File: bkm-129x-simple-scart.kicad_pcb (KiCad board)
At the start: 2 copper layers, 105 x 89.3 mm, 53 parts, among them J1 SCART-F, J2 RCA-RA, J5 Conn_02x32_Row_Letter_Last, Q1 DTC144EKA, U1 ADG1611, U2 THS7374, U3 arduino-nano-v3, U4 74LVC125, U5 MIC3490-3.3

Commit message: Fixed some footprints
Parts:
- added J3: RIGHT, rcj-41x:RCJ-04X, F.Cu at (122.5, 86.4)
- J2: value RCA-RA -> LEFT
- moved J2 75.8 mm to (122.5, 68.6)
- moved J1 33.8 mm to (130.7, 125.2)
- moved R30 32.1 mm to (138.6, 89.5), turned to 270 degrees
- moved R31 32.1 mm to (141.9, 89.5), turned to 90 degrees
- moved R29 32.1 mm to (135.0, 89.6), turned to 270 degrees
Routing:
- net /AUDIO_R: track 15.6 -> 65.7 mm
- net /AUDIO_L: track 27.4 -> 54.7 mm
- net Net-(C4-Pad2): track 53.1 -> 27.8 mm, vias 1 -> 0
- net Net-(C2-Pad2): track 19.8 -> 41.9 mm, vias 0 -> 1
- net Net-(C1-Pad2): track 21.2 -> 37.3 mm, vias 0 -> 1
- net Net-(C3-Pad2): track 36.2 -> 24.7 mm
- net VDD: track 88.4 -> 91.5 mm
- net /AUDIO_MONO: track 30.4 -> 32.4 mm
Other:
- board size 105 x 89.3 mm -> 105 x 90.7 mm
- board text added: "For stereo: R29,31 - Not mounted R30 - 0R (jumper)"
- board text added: "Left/Mono"
- board text added: "R1,18 - 10K R6,7,8,9 - 150R R10,11,12,13 - 75R R19,23 - 4K7 R20,22,25,27 - 100K R21,24,26,28 - 100R R29 - 470R | NM R30 - 470R | 0R R31 - 20K | NM All 0805 size"
- board text added: "Right"
- board text added: "U1 - ADG1611 U2 - THS7374 U3 - Arduino Nano v3 (5V/16MHz) U4 - 74VHC125 U5 - MIC3490-3.3 Q1 - DTC144EKA J2,3 - CUI RCJ-41X U1/2/4: TSSOP14"
- board text removed: "Mono Audio Out"
- board text removed: "R1,18 - 10K R6,7,8,9 - 150R R10,11,12,13 - 75R R19,23 - 4K7 R20,22,25,27 - 100K R21,24,26,28 - 100R R29,30 - 470R R31 - 20K All 0805 size"
- board text removed: "U1 - ADG1611 U2 - THS7374 U3 - Arduino Nano v3 (5V/16MHz) U4 - 74VHC125 U5 - MIC3490-3.3 Q1 - DTC144EKA J2 - CUI RCJ-41X U1/2/4: TSSOP14"

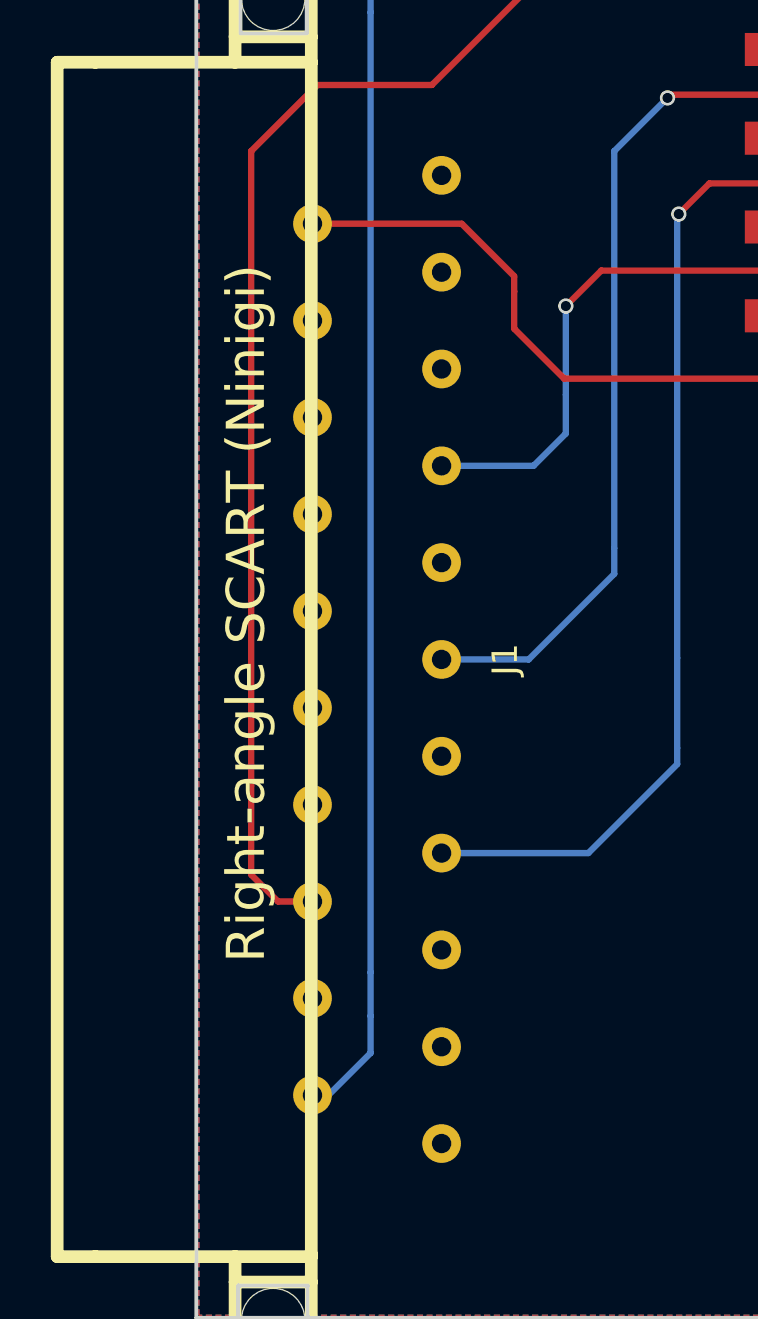
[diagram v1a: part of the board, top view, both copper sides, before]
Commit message: Fixed SCART pad size and added signal names
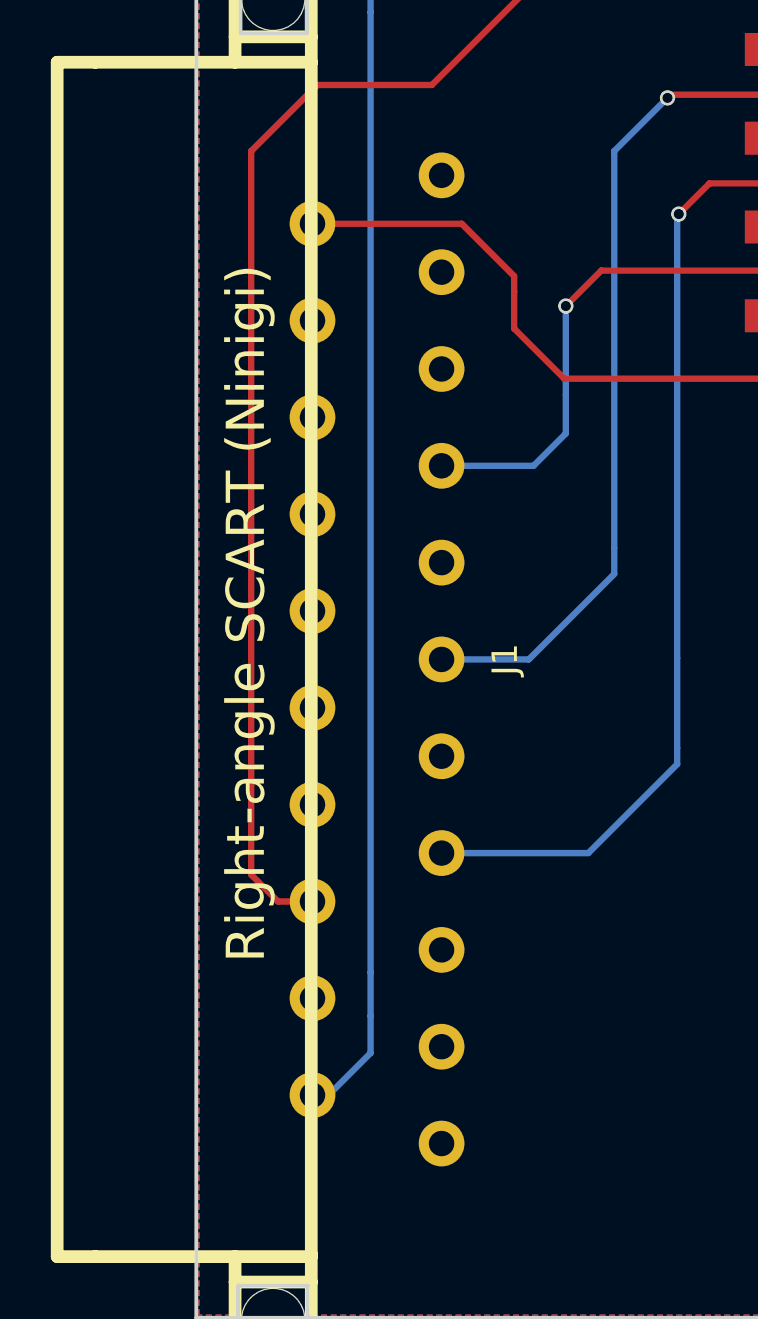
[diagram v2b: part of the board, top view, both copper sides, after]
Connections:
- net Net-(C1-Pad2) renamed /SCART_G
- net Net-(C2-Pad2) renamed /SCART_B
- net Net-(C3-Pad2) renamed /SCART_R
- net Net-(C4-Pad2) renamed /SCART_SYNC

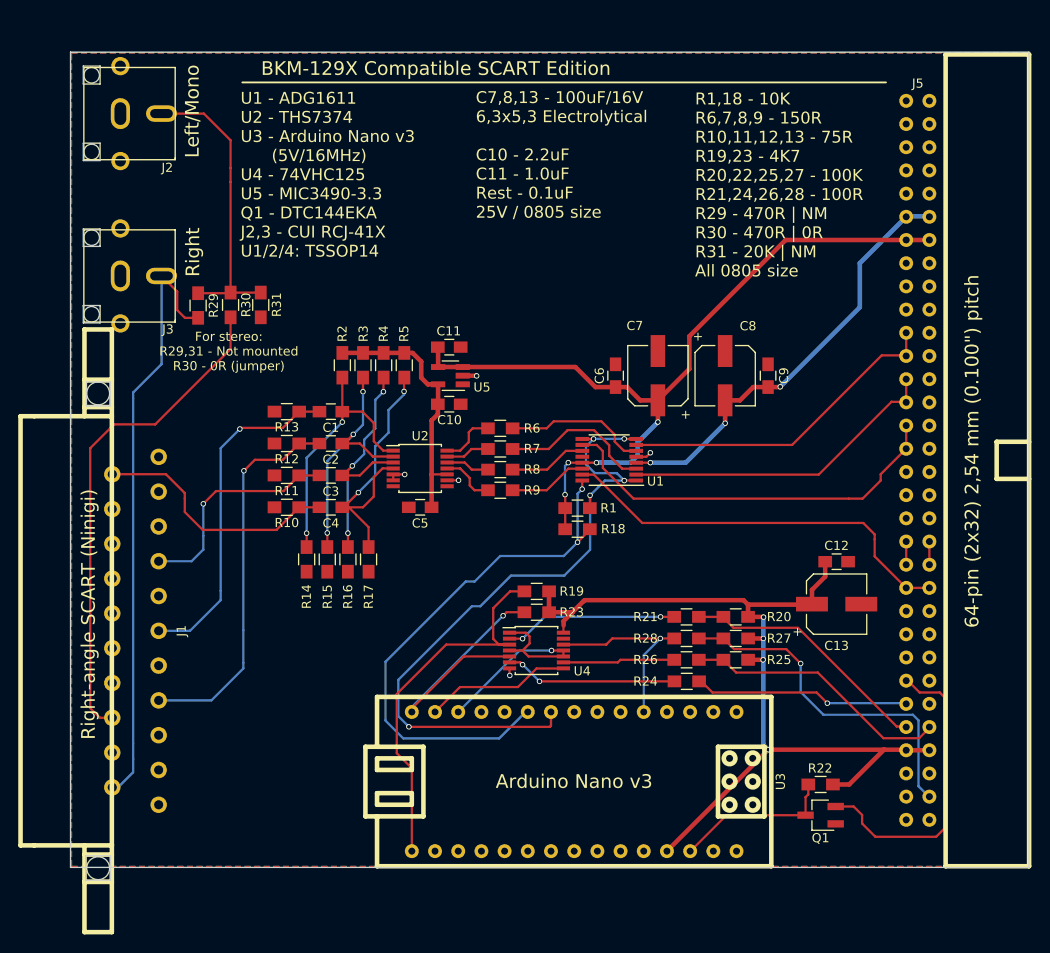
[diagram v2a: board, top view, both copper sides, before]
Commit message: Added audio switch, enlarge holes for SCART fasteners
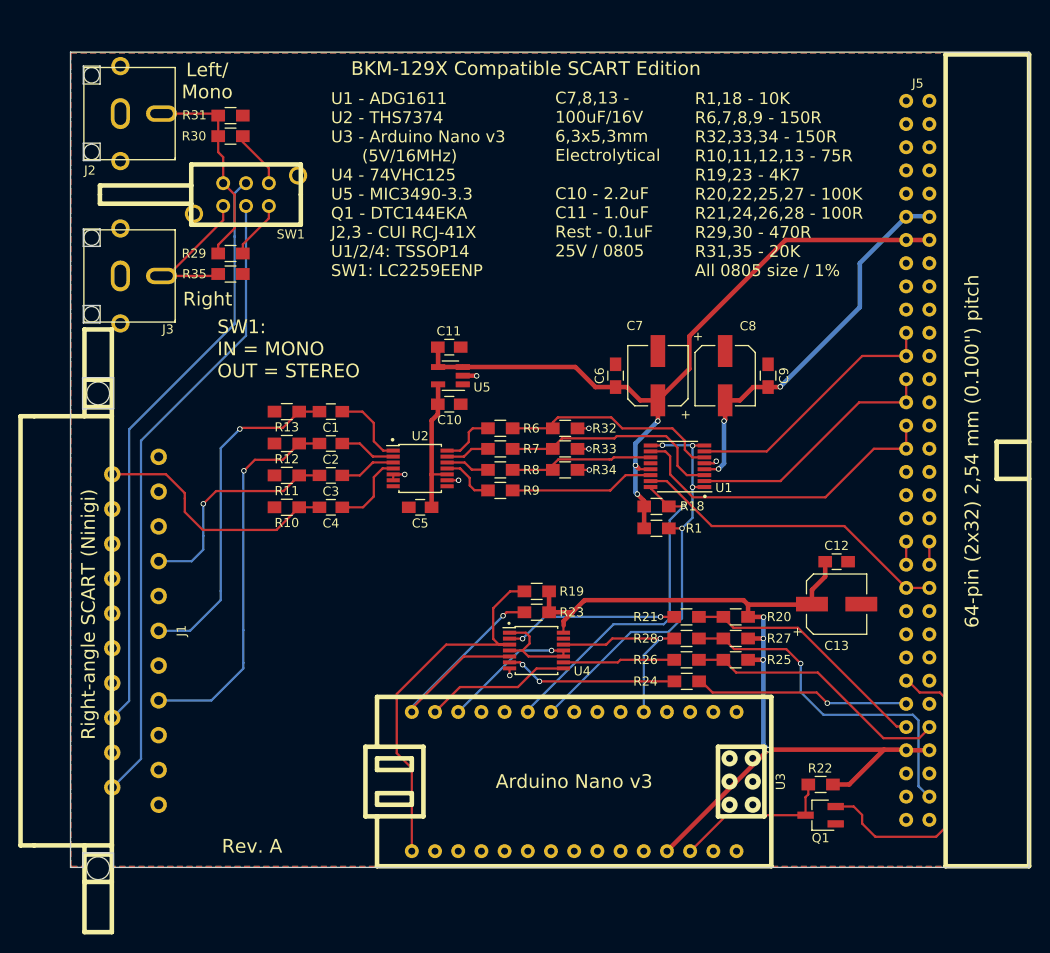
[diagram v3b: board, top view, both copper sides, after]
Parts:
- removed R14, R15, R16, R17, R2, R3, R4, R5: R, Resistors_SMD:R_0805_HandSoldering
- added R32: 150R, Resistors_SMD:R_0805_HandSoldering, F.Cu at (175.2, 103.0)
- added R33: 150R, Resistors_SMD:R_0805_HandSoldering, F.Cu at (175.2, 105.3)
- added R34: 150R, Resistors_SMD:R_0805_HandSoldering, F.Cu at (175.2, 107.6)
- added R35: 20K, Resistors_SMD:R_0805_HandSoldering, F.Cu at (138.6, 86.2)
- added SW1: LC2259EENP, LC2259:LC2259, F.Cu at (140.2, 77.5)
- R9: value 150R -> 0R
- moved R31 21.0 mm to (138.6, 68.8), turned to 180 degrees
- moved R30 18.5 mm to (138.6, 71.0), turned to 0 degrees
- moved R18 9.00 mm to (185.2, 111.6)
- moved R1 8.92 mm to (185.2, 114.0)
- moved U1 7.51 mm to (187.5, 107.2)
- moved R29 6.71 mm to (138.6, 83.9), turned to 0 degrees
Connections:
- net /AUDIO_MONO renamed Net-(J2-Pad1)
- J3 pad 1: /AUDIO_R -> Net-(J3-Pad1)
- R29 pad 2: /AUDIO_R -> Net-(R29-Pad2)
- R30 pad 2: /AUDIO_L -> Net-(R30-Pad2)
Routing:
- net ~BX_OE: track 76.7 -> 46.7 mm, vias 5 -> 4
- net Net-(C4-Pad1): track 31.6 -> 9.44 mm, vias 2 -> 0
- net ~EXT_SYNC_OE: track 59.4 -> 37.6 mm, vias 2 -> 1
- net Net-(C2-Pad1): track 28.5 -> 6.77 mm, vias 3 -> 0
- net Net-(C3-Pad1): track 27.9 -> 6.23 mm, vias 3 -> 0
- net Net-(C1-Pad1): track 28.7 -> 8.51 mm, vias 2 -> 0
- net Net-(J3-Pad1): track 0.00 -> 17.4 mm
- net +3V3: track 29.0 -> 16.0 mm
- net /AUDIO_L: track 54.7 -> 64.7 mm
- net Net-(J2-Pad1): track 32.4 -> 22.9 mm
- net /EXT_SYNC: track 44.6 -> 35.4 mm
- net Net-(R32-Pad1): track 15.6 -> 24.3 mm
- net /P-R/R: track 44.2 -> 36.0 mm
- net Net-(R33-Pad1): track 16.8 -> 24.7 mm
- net Net-(R34-Pad1): track 8.48 -> 16.0 mm
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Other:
- board size 105 x 90.7 mm -> 105 x 89.3 mm
- board text added: "C7,8,13 - 100uF/16V 6,3x5,3mm Electrolytical C10 - 2.2uF C11 - 1.0uF Rest - 0.1uF 25V / 0805"
- board text added: "Left/ Mono"
- board text added: "R1,18 - 10K R6,7,8,9 - 150R R32,33,34 - 150R R10,11,12,13 - 75R R19,23 - 4K7 R20,22,25,27 - 100K R21,24,26,28 - 100R R29,30 - 470R R31,35 - 20K All 0805 size / 1%"
- board text added: "Rev. A"
- board text added: "SW1: IN = MONO OUT = STEREO"
- board text added: "U1 - ADG1611 U2 - THS7374 U3 - Arduino Nano v3 (5V/16MHz) U4 - 74VHC125 U5 - MIC3490-3.3 Q1 - DTC144EKA J2,3 - CUI RCJ-41X U1/2/4: TSSOP14 SW1: LC2259EENP"
- board text removed: "C7,8,13 - 100uF/16V 6,3x5,3 Electrolytical C10 - 2.2uF C11 - 1.0uF Rest - 0.1uF 25V / 0805 size"
- board text removed: "For stereo: R29,31 - Not mounted R30 - 0R (jumper)"
- board text removed: "Left/Mono"
- board text removed: "R1,18 - 10K R6,7,8,9 - 150R R10,11,12,13 - 75R R19,23 - 4K7 R20,22,25,27 - 100K R21,24,26,28 - 100R R29 - 470R | NM R30 - 470R | 0R R31 - 20K | NM All 0805 size"
- board text removed: "U1 - ADG1611 U2 - THS7374 U3 - Arduino Nano v3 (5V/16MHz) U4 - 74VHC125 U5 - MIC3490-3.3 Q1 - DTC144EKA J2,3 - CUI RCJ-41X U1/2/4: TSSOP14"

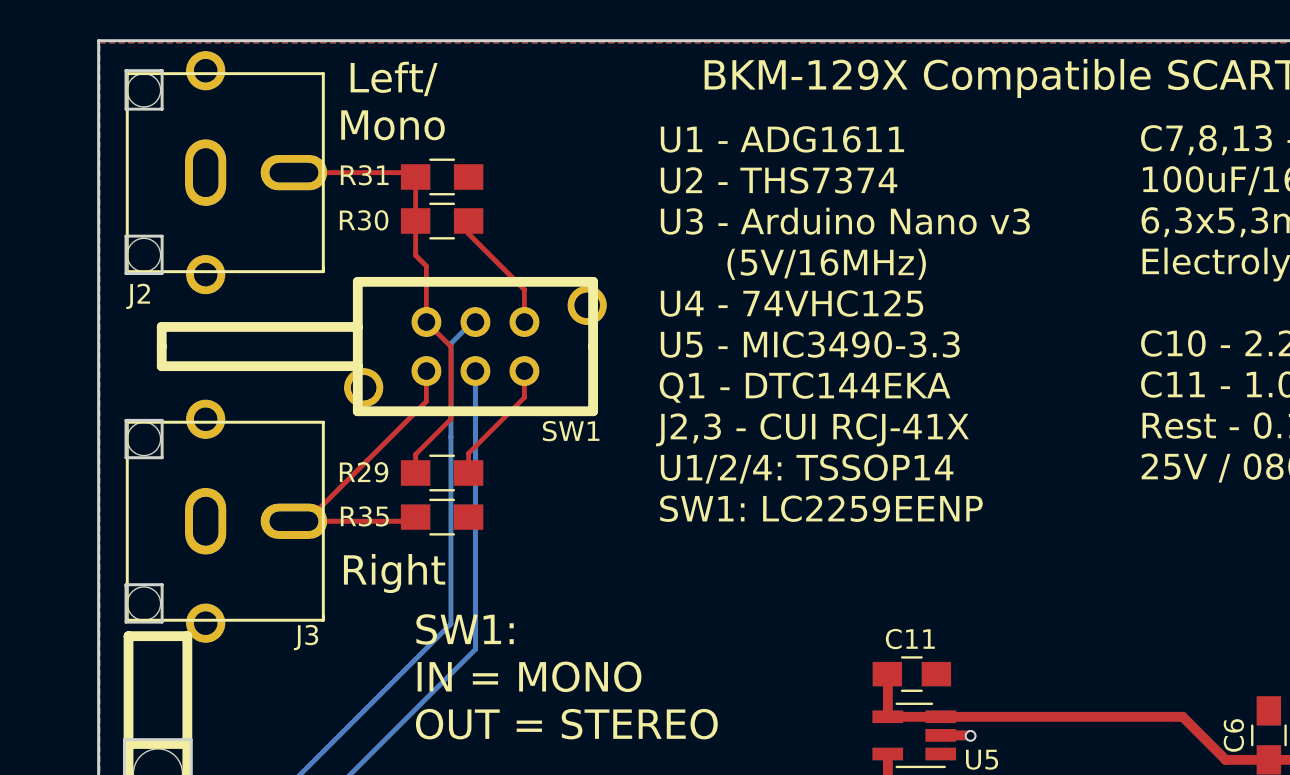
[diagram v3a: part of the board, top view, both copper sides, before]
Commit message: Fixed erroneous RCA plug part number
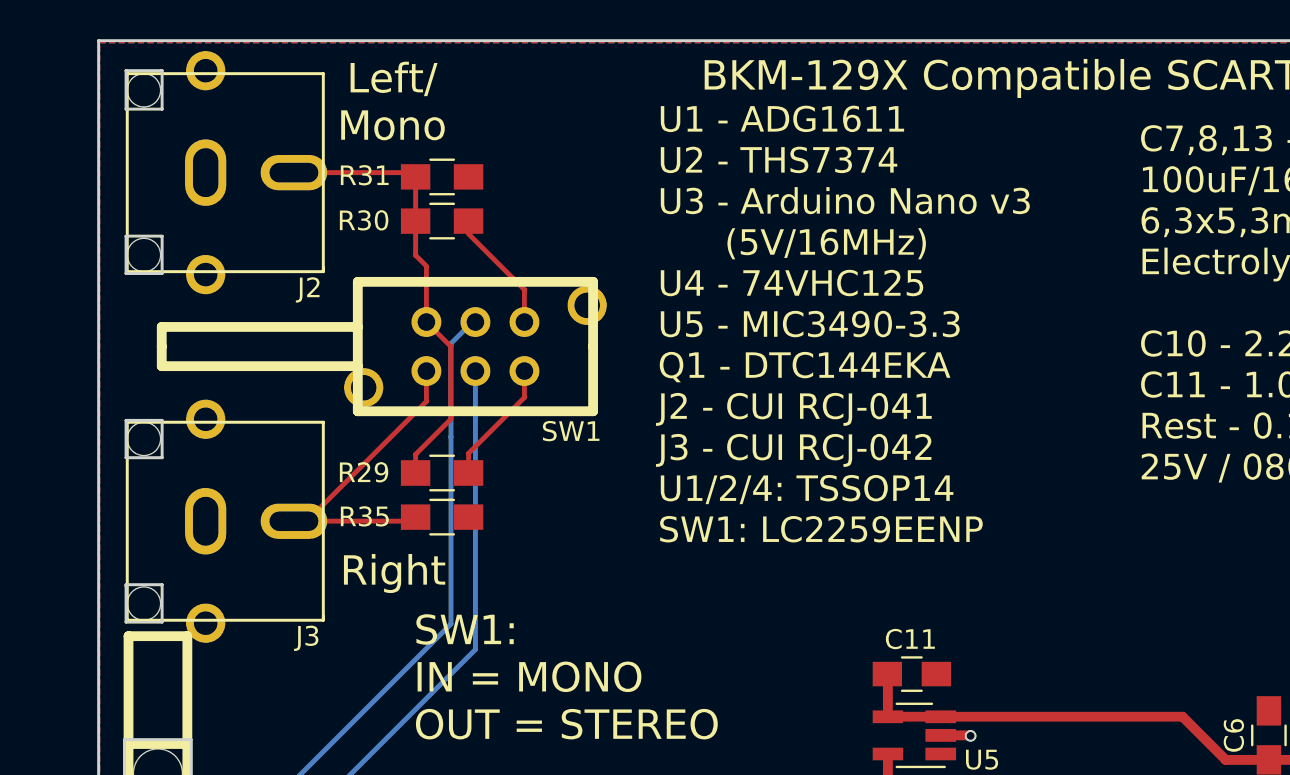
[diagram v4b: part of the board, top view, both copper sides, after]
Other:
- board text added: "U1 - ADG1611 U2 - THS7374 U3 - Arduino Nano v3 (5V/16MHz) U4 - 74VHC125 U5 - MIC3490-3.3 Q1 - DTC144EKA J2 - CUI RCJ-041 J3 - CUI RCJ-042 U1/2/4: TSSOP14 SW1: LC2259EENP"
- board text removed: "U1 - ADG1611 U2 - THS7374 U3 - Arduino Nano v3 (5V/16MHz) U4 - 74VHC125 U5 - MIC3490-3.3 Q1 - DTC144EKA J2,3 - CUI RCJ-41X U1/2/4: TSSOP14 SW1: LC2259EENP"
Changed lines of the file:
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@@
     (links 161)
     (no_connects 0)
-    (area 120.954999 61.773999 226.075001 151.205001)
+    (area 112.716499 61.652999 226.459201 158.672001)
     (thickness 1.6)
     (drawings 44)
@@
   (module rcj-41x:RCJ-04X (layer F.Cu)
     (at 122.4915 86.36 180)
-    (fp_text reference J3 (at -9.2075 -5.842 180) (layer F.SilkS)
+    (fp_text reference J3 (at -9.2185 -5.88 180) (layer F.SilkS)
       (effects (font (size 1 1) (thickness 0.15)))
     )
@@
   (module rcj-41x:RCJ-04X (layer F.Cu)
     (at 122.4915 68.58 180)
-    (fp_text reference J2 (at -0.6585 -6.22 180) (layer F.SilkS)
+    (fp_text reference J2 (at -9.3085 -5.89 180) (layer F.SilkS)
       (effects (font (size 1 1) (thickness 0.15)))
     )
@@
     (effects (font (size 1.3 1.3) (thickness 0.25)) (justify left))
   )
-  (gr_text "U1 - ADG1611\nU2 - THS7374\nU3 - Arduino Nano v3\n      (5V/16MHz)\nU4 - 74VHC125\nU5 - MIC3490-3.3\nQ1 - DTC144EKA\nJ2,3 - CUI RCJ-41X\nU1/2/4: TSSOP14\nSW1: LC2259EENP" (at 149.55 76.35) (layer F.SilkS)
+  (gr_text "U1 - ADG1611\nU2 - THS7374\nU3 - Arduino Nano v3\n      (5V/16MHz)\nU4 - 74VHC125\nU5 - MIC3490-3.3\nQ1 - DTC144EKA\nJ2 - CUI RCJ-041\nJ3 - CUI RCJ-042\nU1/2/4: TSSOP14\nSW1: LC2259EENP" (at 149.55 76.35) (layer F.SilkS)
     (effects (font (size 1.3 1.3) (thickness 0.25)) (justify left))
   )
